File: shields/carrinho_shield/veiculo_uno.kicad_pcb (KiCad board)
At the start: 2 copper layers, 68.6 x 53.3 mm, 39 parts, among them J1 Conn_01x02_Male, J10 Conn_01x02_Male, J11 Conn_01x02_Male, J12 Conn_01x02_Male, J13 Conn_01x02_Male, J14 Conn_01x02_Male, J15 Conn_01x02_Male, J16 Conn_01x02_Male, J17 Conn_01x02_Male, J18 Conn_01x02_Male, J19 Conn_01x02_Male, J2 Conn_01x02_Male, J20 Conn_01x02_Male, J21 Conn_01x02_Male, J23 Conn_01x04_Male, J3 Conn_01x02_Male, J4 Conn_01x02_Male, J5 Conn_01x02_Male, J6 Conn_01x02_Male, J7 Conn_02x13_Odd_Even, J8 Conn_01x02_Male, J9 Conn_01x02_Male, P1 Power, P2 Analog, P3 Digital, P4 Digital, P6 CONN_01X01, P7 CONN_01X01, P8 CONN_01X01, Q1 2N7002, Q2 2N7002

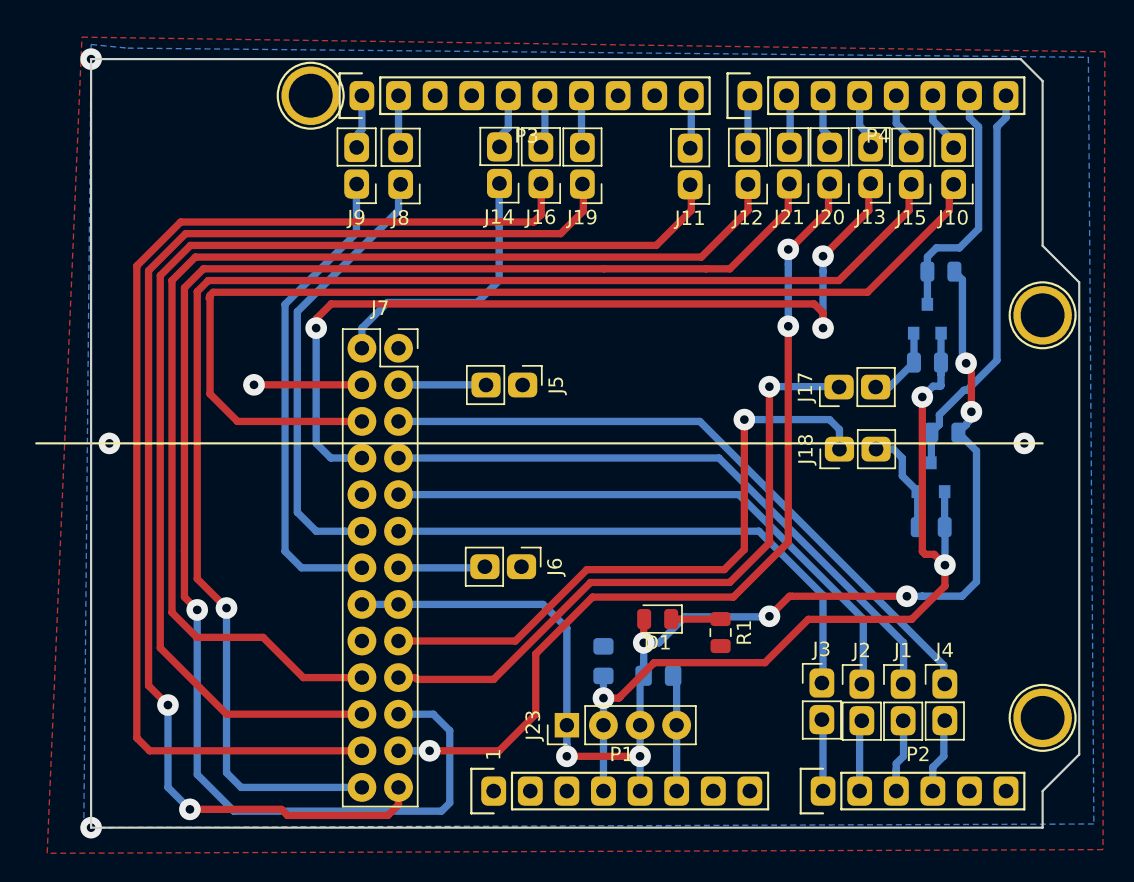
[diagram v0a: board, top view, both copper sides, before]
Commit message: Added diode in +5V.
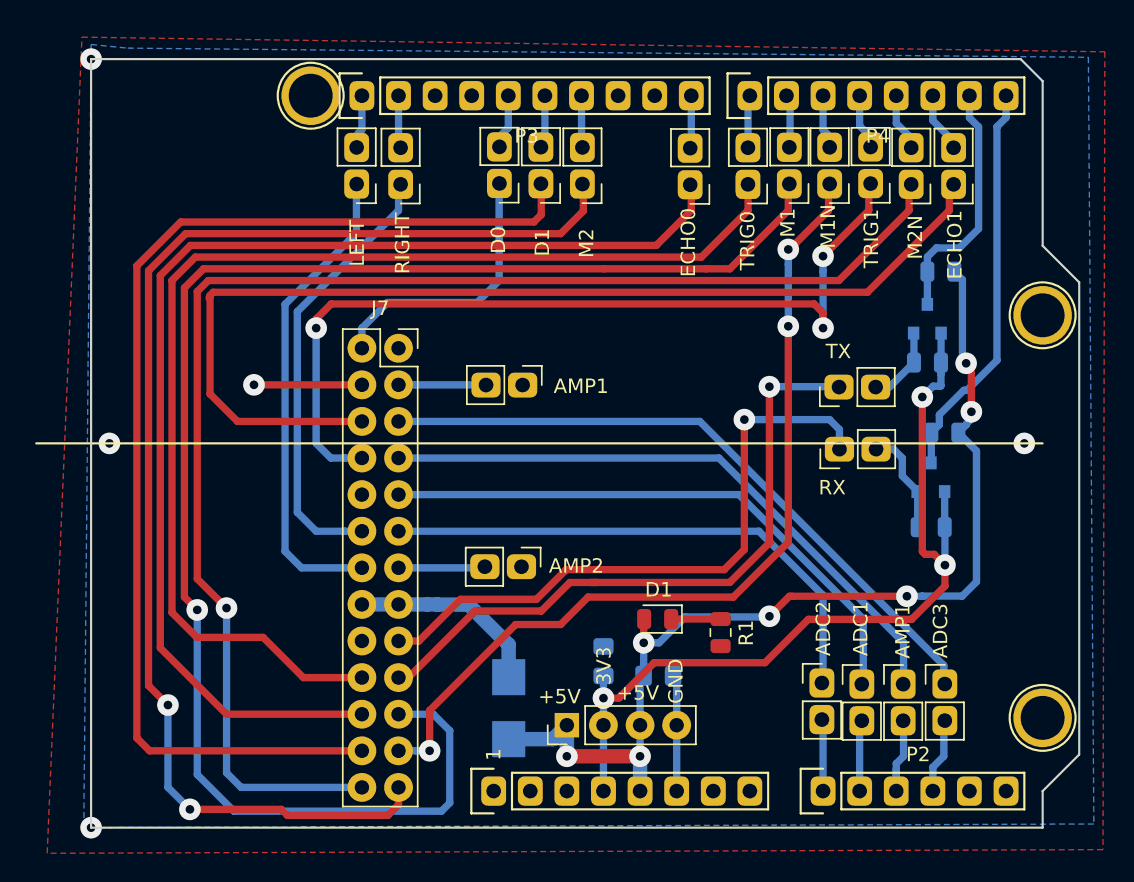
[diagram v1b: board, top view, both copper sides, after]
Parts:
- added D2: D_Schottky, Diode_SMD:D_SMB, B.Cu at (140.0, 118.1)
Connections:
- J7 pad 15: +5V -> +5VP
- J7 pad 16: +5V -> +5VP
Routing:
- net +5V: track 86.9 -> 72.3 mm
- net +5VP: track 0.00 -> 13.6 mm
- net PWM1N: track 61.1 -> 60.3 mm
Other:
- net class POWER added: clearance 0.3048, trace_width 1, via_dia 1.5, via_drill 0.6
- board text added: "+5V"
- board text added: "3V3"
- board text added: "ADC1"
- board text added: "ADC2"
- board text added: "ADC3"
- board text added: "AMP1"
- board text added: "AMP2"
- board text added: "D0"
- board text added: "D1"
- board text added: "ECHO0"
- board text added: "ECHO1"
- board text added: "GND"
- board text added: "LEFT"
- board text added: "M1"
- board text added: "M1N"
- board text added: "M2"
- board text added: "M2N"
- board text added: "RIGHT"
- board text added: "RX"
- board text added: "TRIG0"
- board text added: "TRIG1"
- board text added: "TX"

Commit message: Change 26 pins connector
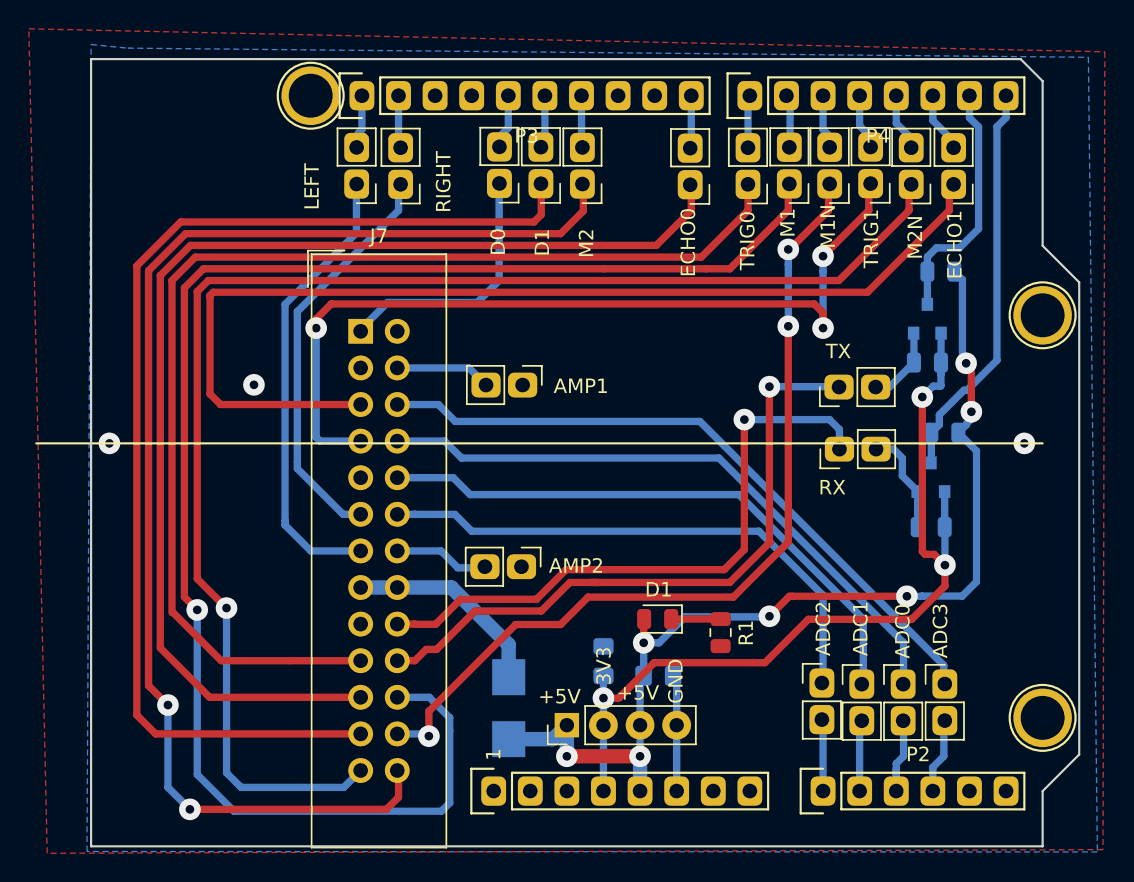
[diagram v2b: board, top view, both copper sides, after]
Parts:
- J7: footprint Connector_PinSocket_2.54mm:PinSocket_2x13_P2.54mm_Vertical -> Connector_IDC:IDC-Header_2x13_P2.54mm_Vertical
- moved J7 2.88 mm to (129.7, 91.9)
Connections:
- J7 pad 1: GND -> D0
- J7 pad 10: Net-(J7-Pad10) -> ADC1
- J7 pad 11: ADC2 -> R_TCRT
- J7 pad 12: R_TCRT -> ADC2
- J7 pad 13: AMP2 -> L_TCRT
- J7 pad 14: L_TCRT -> AMP2
- J7 pad 17: TXB -> GND
- J7 pad 18: GND -> TXB
- J7 pad 19: RXB -> Trig0
- J7 pad 2: D0 -> GND
- J7 pad 20: Trig0 -> RXB
- J7 pad 21: PWM1 -> Echo0
- J7 pad 22: Echo0 -> PWM1
- J7 pad 23: PWM1N -> D1
- J7 pad 24: D1 -> PWM1N
- J7 pad 25: PWM2 -> PWM2N
- J7 pad 26: PWM2N -> PWM2
- J7 pad 3: AMP1 -> GND
- J7 pad 4: GND -> AMP1
- J7 pad 5: ADC3 -> Echo1
- J7 pad 6: Echo1 -> ADC3
- J7 pad 7: ADC0 -> Trig1
- J7 pad 8: Trig1 -> ADC0
- J7 pad 9: ADC1 -> Net-(J7-Pad9)
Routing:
- net GND: track 16.1 -> 8.64 mm
- net R_TCRT: track 30.2 -> 27.9 mm
- net L_TCRT: track 32.9 -> 31.2 mm
- net D1: track 79.9 -> 78.4 mm
- net D0: track 18.5 -> 17.1 mm
- net PWM1: track 107.5 -> 108.6 mm
- net PWM1N: track 60.3 -> 59.4 mm
- net Trig1: track 60.0 -> 59.2 mm
- net AMP1: track 5.97 -> 6.65 mm
- net Echo1: track 73.4 -> 72.7 mm
- net ADC3: track 46.2 -> 46.8 mm
- net ADC2: track 37.5 -> 38.1 mm
- net ADC0: track 43.3 -> 43.9 mm
- net Echo0: track 81.8 -> 81.3 mm
- net ADC1: track 40.4 -> 41.0 mm
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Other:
- board size 68.6 x 53.3 mm -> 68.6 x 54.6 mm
- board text added: "ADC0"

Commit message: Added PCB labels
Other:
- board text added: "Shield Arduino Uno Prof. Renan Augusto Starke"
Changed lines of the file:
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@@
   (general
     (thickness 1.6)
-    (drawings 56)
+    (drawings 57)
     (tracks 330)
     (zones 0)
@@
     (visible_elements FFFFFF7F)
     (pcbplotparams
-      (layerselection 0x01000_ffffffff)
+      (layerselection 0x01030_ffffffff)
       (usegerberextensions false)
       (usegerberattributes false)
@@
     )
   )
+  (gr_text "Shield Arduino Uno\nProf. Renan Augusto Starke" (at 147.828 102.235) (layer F.SilkS)
+    (effects (font (size 1 1) (thickness 0.1)))
+  )
   (gr_text GND (at 151.5872 116.205 90) (layer F.SilkS)
